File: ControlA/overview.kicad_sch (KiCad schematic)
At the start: 0 parts

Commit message: add libray symbole and add sheet
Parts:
- added C? (x2): 100n, symbol Device:C
- added C? (x2): C_Polarized_US, symbol Device:C_Polarized_US
- added D?: LED, symbol Device:LED
- added D?: SMAJ6.0CA, SMAJ6.0CA:DIOM4325X250N, symbol SMAJ60CA:SMAJ6.0CA
- added J?: XT30PW-M, XT30PW-M:AMASS_XT30PW-M, symbol XT30PW_M:XT30PW-M
- added R? (x2): 2K2, symbol Device:R
- added R? (x2): 39K, symbol Device:R
- added TH?: 10K, symbol Device:Thermistor_NTC
- added U?: XH-2PWBPZ, symbol XH-2PWBPZ:XH-2PWBPZ
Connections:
- new net: D?.2 (A), R?.2
- new net +3V3: C?.1, R?.1, U?.1
- new net +VDC: C?.1, C?.1, D?.1, J?.P, R?.1, R?.1
- new net ADC_TEMP: R?.2, TH?.1, U?.2
- new net AN_JN: C?.1, R?.1, R?.2
- new net GND: C?.2, C?.2, C?.2, C?.2, D?.1 (K), D?.2, J?.N, R?.2, TH?.2
- no-connect marks 0 -> 2
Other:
- note added: "BULK CAPACITANCE"
- note added: "CAN BE USED AS SENSOR ON THE BOARD OR SENSOR ON THE MOTOR"
- note added: "ESD SURGE PROTECTION"
- note added: "LED GREEN -POWER ON INDICATOR"
- note added: "NTC THERMISTOR"
- note added: "VOLTAGE_DIVIDER"
- note added: "WHEN: VDC=60V => AN_JN = 3V204"
- note added: "place as close as possible to THE DRIVER MOSFETS"
- note added: "place as close as possible to connector"

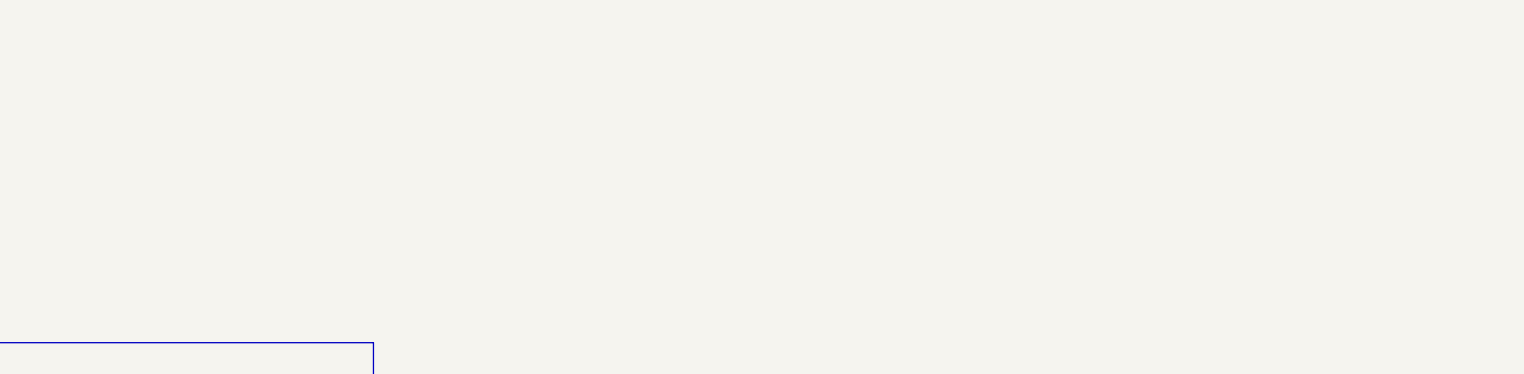
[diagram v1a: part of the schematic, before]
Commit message: shema input protection final
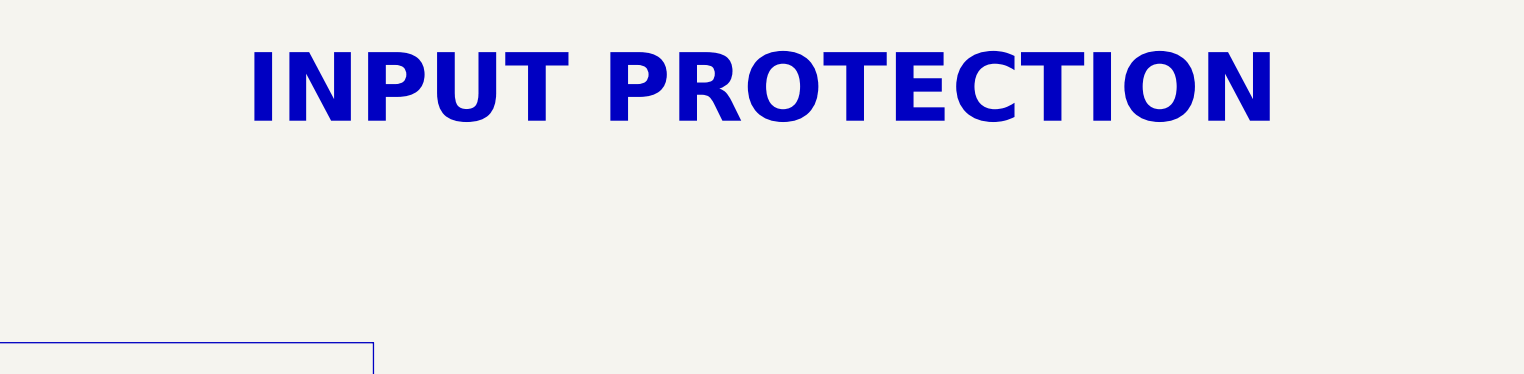
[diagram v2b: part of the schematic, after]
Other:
- note added: "INPUT PROTECTION"
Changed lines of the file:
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@@
+		)
+	)
+	(text "INPUT PROTECTION "
+		(exclude_from_sim no)
+		(at 146.05 35.56 0)
+		(effects
+			(font
+				(face "Arial Black")
+				(size 7.62 7.62)
+				(bold yes)
+				(color 0 0 0 1)
+			)
 		)
 	)

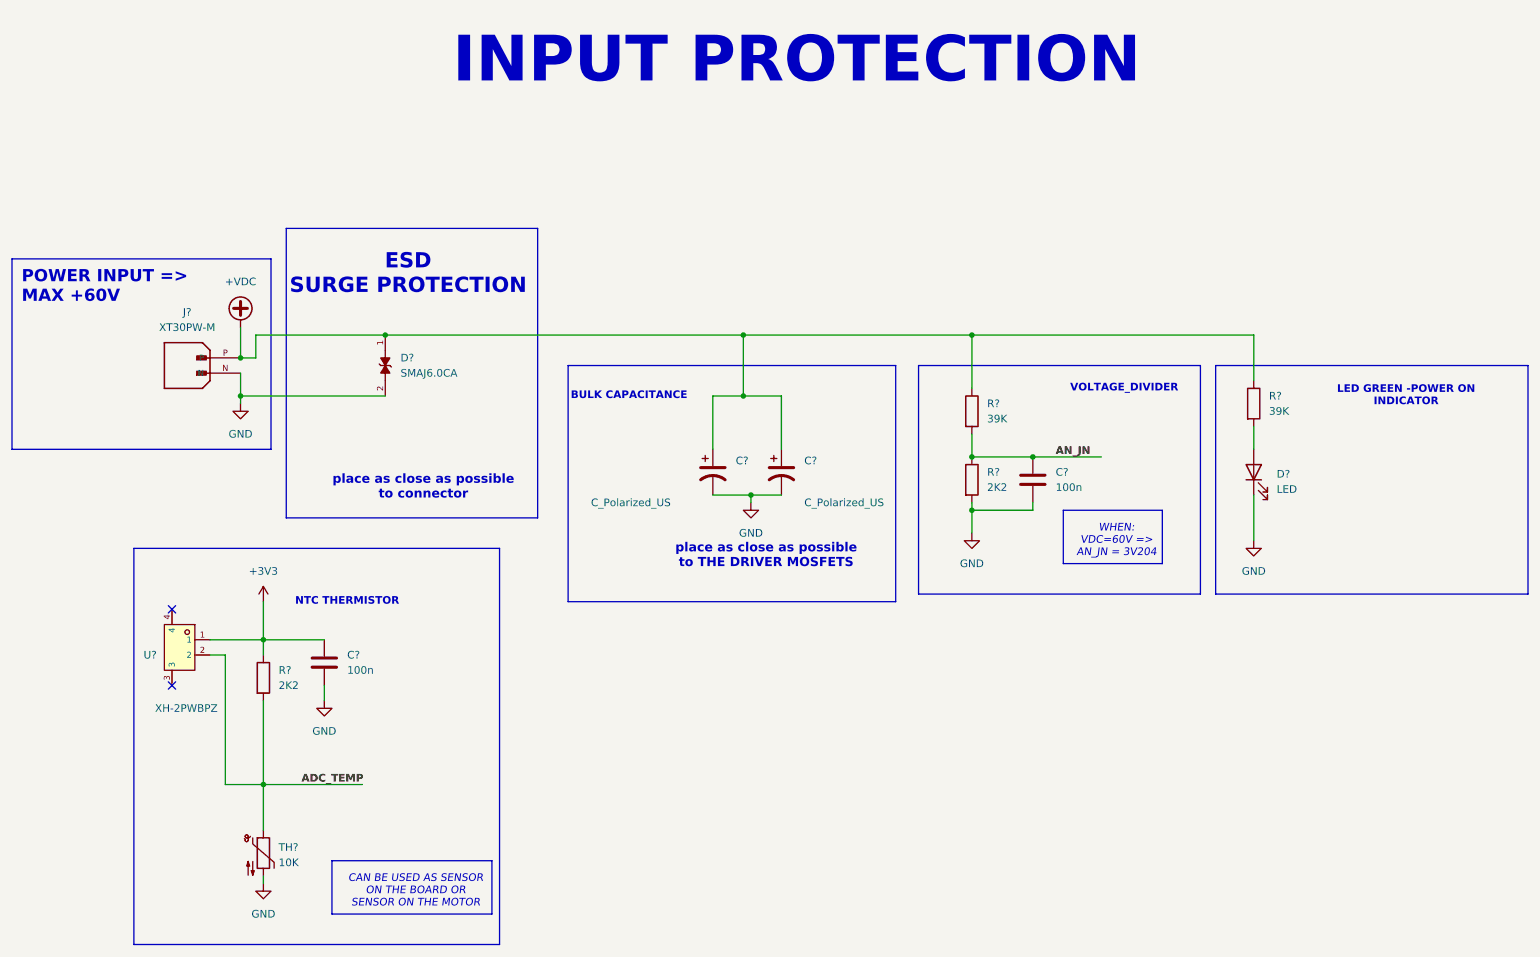
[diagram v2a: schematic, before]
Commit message: final shema symbole
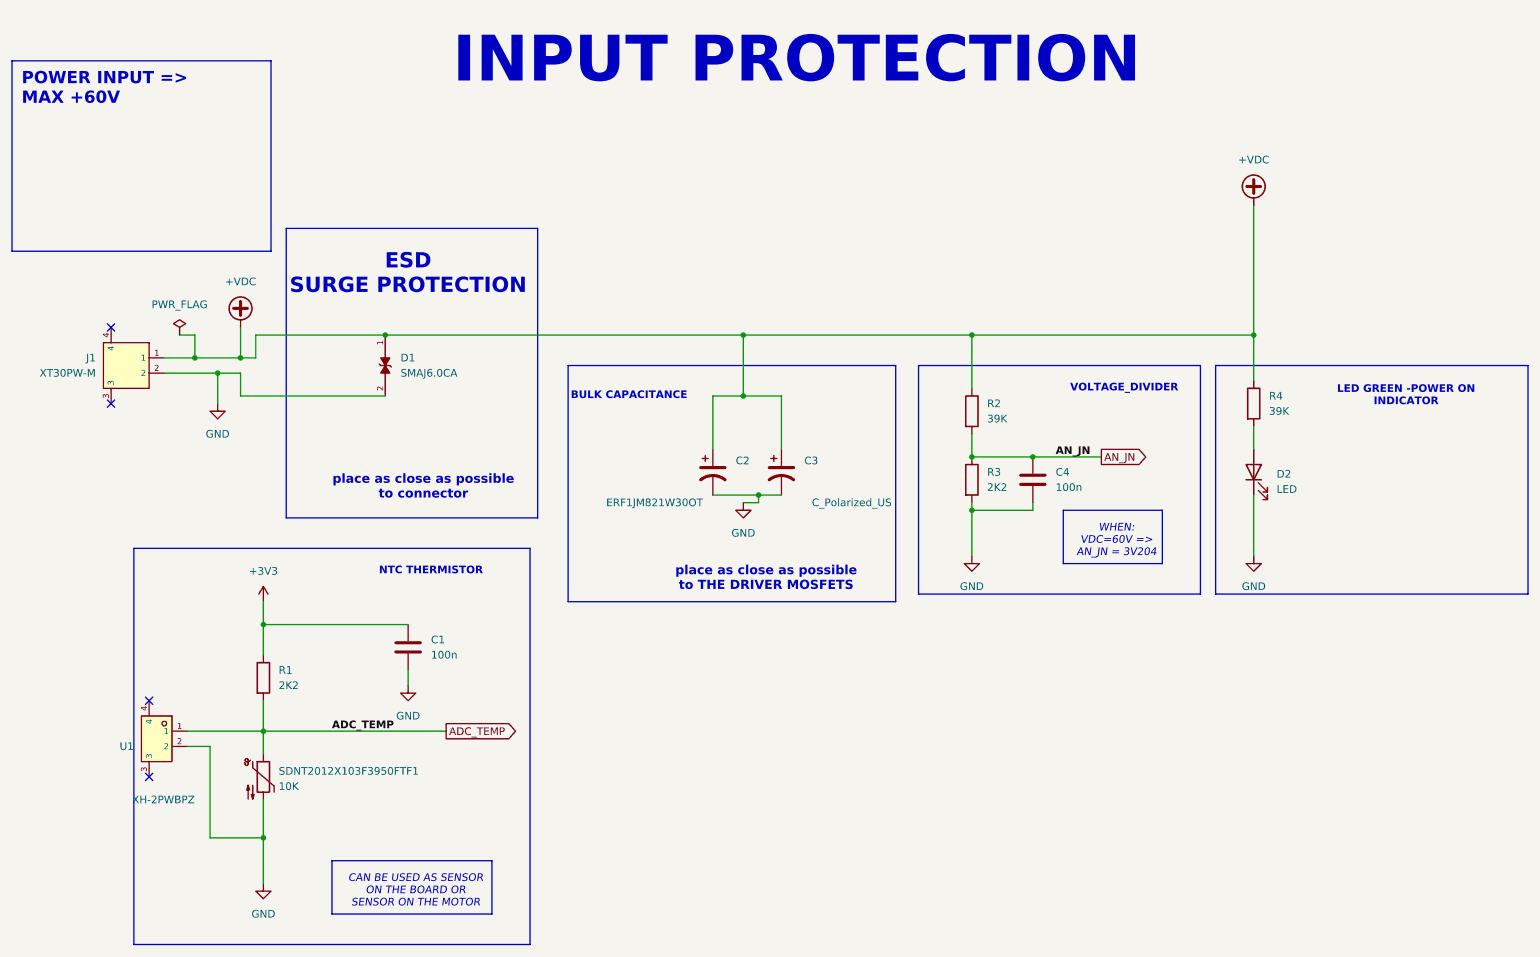
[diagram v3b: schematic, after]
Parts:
- removed C? (x2): C_Polarized_US, symbol Device:C_Polarized_US
- added C2: ERF1JM821W30OT, Capacitor_THT:CP_Radial_D12.5mm_P5.00mm, symbol Device:C_Polarized_US
- added C3: C_Polarized_US, Capacitor_THT:CP_Radial_D12.5mm_P5.00mm, symbol Device:C_Polarized_US
- C1, C4: renamed from C?; footprint (none) -> Capacitor_SMD:C_0805_2012Metric
- D1: renamed from D?; footprint SMAJ6.0CA:DIOM4325X250N -> footprint:DIOM4325X250N
- D2: renamed from D?; footprint (none) -> footprint:LED0805-R-RD
- J1: renamed from J?; footprint XT30PW-M:AMASS_XT30PW-M -> footprint:CONN-TH_XT30PW-M; LCSC (none) -> C431092
- R1, R2, R3, R4: renamed from R?; footprint (none) -> Resistor_SMD:R_0805_2012Metric
- SDNT2012X103F3950FTF1: renamed from TH?; footprint (none) -> Resistor_SMD:R_0805_2012Metric
- U1: renamed from U?; footprint (none) -> footprint:CONN-SMD_XH-2PWBPZ
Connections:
- net +3V3: no longer U1.1
- net +VDC: now also J1.1, C2.1, C3.1; no longer J1.P
- net ADC_TEMP: now also U1.1; no longer U1.2
- net GND: now also J1.2, U1.2, C2.2, C3.2; no longer J1.N
- no-connect marks 2 -> 4
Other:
- moved on the sheet: C1, SDNT2012X103F3950FTF1, U1

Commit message: test0
FIREST
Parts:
- C3: value C_Polarized_US -> ERF1JM821W30OT
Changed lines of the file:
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@@
 			)
 		)
-		(property "Value" "C_Polarized_US"
+		(property "Value" "ERF1JM821W30OT"
 			(at 148.59 109.22 0)
 			(effects

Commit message: CHANGE V11
change v1
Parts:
- C4: footprint Capacitor_SMD:C_0805_2012Metric -> Capacitor_SMD:C_0603_1608Metric
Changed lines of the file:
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@@
-	(wire
-		(pts
-			(xy 137.16 109.22) (xy 139.7 109.22)
-		)
-		(stroke
-			(width 0)
-			(type default)
-		)
-	)
 	(wire
 		(pts
@@
 	(wire
 		(pts
+			(xy 57.15 165.1) (xy 57.15 172.72)
+		)
+		(stroke
+			(width 0)
+			(type default)
+		)
+	)
+	(wire
+		(pts
 			(xy 137.16 81.28) (xy 175.26 81.28)
 		)
@@
 	(wire
 		(pts
-			(xy 139.7 109.22) (xy 139.7 107.95)
+			(xy 139.7 111.76) (xy 139.7 107.95)
 		)
 		(stroke
@@
 		(pts
 			(xy 45.72 85.09) (xy 53.34 85.09)
-		)
-		(stroke
-			(width 0)
-			(type default)
-		)
-	)
-	(wire
-		(pts
-			(xy 57.15 165.1) (xy 57.15 172.72)
 		)
 		(stroke
@@
 	)
 	(symbol
-		(lib_id "power:GND")
-		(at 57.15 172.72 0)
-		(unit 1)
-		(exclude_from_sim no)
-		(in_bom yes)
-		(on_board yes)
-		(dnp no)
-		(fields_autoplaced yes)
-		(property "Reference" "#PWR059"
-			(at 57.15 179.07 0)
-			(effects
-				(font
-					(size 1.27 1.27)
-				)
-				(hide yes)
-			)
-		)
-		(property "Value" "GND"
-			(at 57.15 177.8 0)
-			(effects
-				(font
-					(size 1.27 1.27)
-				)
-			)
-		)
-		(property "Footprint" ""
-			(at 57.15 172.72 0)
-			(effects
-				(font
-					(size 1.27 1.27)
-				)
-				(hide yes)
-			)
-		)
-		(property "Datasheet" ""
-			(at 57.15 172.72 0)
-			(effects
-				(font
-					(size 1.27 1.27)
-				)
-				(hide yes)
-			)
-		)
-		(property "Description" "Power symbol creates a global label with name \"GND\" , ground"
-			(at 57.15 172.72 0)
-			(effects
-				(font
-					(size 1.27 1.27)
-				)
-				(hide yes)
-			)
-		)
-		(pin "1"
-		)
-		(instances
-			(project "ControlA"
-				(path "/28f77b05-53a5-4f29-9b4d-d18dbf030970/8b90f1aa-83f4-48c7-b45b-eecece8cbc1b"
-					(reference "#PWR059")
-					(unit 1)
-				)
-			)
-		)
-	)
-	(symbol
 		(lib_id "Device:C_Polarized_US")
 		(at 143.51 104.14 0)
@@
 	(symbol
 		(lib_id "power:GND")
-		(at 137.16 109.22 0)
+		(at 139.7 111.76 0)
 		(unit 1)
 		(exclude_from_sim no)
@@
 		(fields_autoplaced yes)
 		(property "Reference" "#PWR056"
-			(at 137.16 115.57 0)
+			(at 139.7 118.11 0)
 			(effects
 				(font
@@
 		)
 		(property "Value" "GND"
-			(at 137.16 114.3 0)
+			(at 139.7 116.84 0)
 			(effects
 				(font
@@
 		)
 		(property "Footprint" ""
-			(at 137.16 109.22 0)
+			(at 139.7 111.76 0)
 			(effects
 				(font
@@
 		)
 		(property "Datasheet" ""
-			(at 137.16 109.22 0)
+			(at 139.7 111.76 0)
 			(effects
 				(font
@@
 		)
 		(property "Description" "Power symbol creates a global label with name \"GND\" , ground"
-			(at 137.16 109.22 0)
+			(at 139.7 111.76 0)
 			(effects
 				(font
@@
 	)
 	(symbol
+		(lib_id "power:GND")
+		(at 57.15 172.72 0)
+		(unit 1)
+		(exclude_from_sim no)
+		(in_bom yes)
+		(on_board yes)
+		(dnp no)
+		(fields_autoplaced yes)
+		(property "Reference" "#PWR054"
+			(at 57.15 179.07 0)
+			(effects
+				(font
+					(size 1.27 1.27)
+				)
+				(hide yes)
+			)
+		)
+		(property "Value" "GND"
+			(at 57.15 177.8 0)
+			(effects
+				(font
+					(size 1.27 1.27)
+				)
+			)
+		)
+		(property "Footprint" ""
+			(at 57.15 172.72 0)
+			(effects
+				(font
+					(size 1.27 1.27)
+				)
+				(hide yes)
+			)
+		)
+		(property "Datasheet" ""
+			(at 57.15 172.72 0)
+			(effects
+				(font
+					(size 1.27 1.27)
+				)
+				(hide yes)
+			)
+		)
+		(property "Description" "Power symbol creates a global label with name \"GND\" , ground"
+			(at 57.15 172.72 0)
+			(effects
+				(font
+					(size 1.27 1.27)
+				)
+				(hide yes)
+			)
+		)
+		(pin "1"
+		)
+		(instances
+			(project "ControlA"
+				(path "/28f77b05-53a5-4f29-9b4d-d18dbf030970/8b90f1aa-83f4-48c7-b45b-eecece8cbc1b"
+					(reference "#PWR054")
+					(unit 1)
+				)
+			)
+		)
+	)
+	(symbol
 		(lib_id "Device:C_Polarized_US")
 		(at 132.08 104.14 0)
@@
 			)
 		)
-		(property "Footprint" "Capacitor_SMD:C_0805_2012Metric"
+		(property "Footprint" "Capacitor_SMD:C_0603_1608Metric"
 			(at 186.3852 109.22 0)
 			(effects

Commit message: connector
add conctor power mosft
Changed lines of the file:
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@@
+	)
+	(junction
+		(at 50.8 165.1)
+		(diameter 0)
+		(color 0 0 0 0)
 	)
 	(junction
@@
 	)
 	(junction
-		(at 57.15 165.1)
-		(diameter 0)
-		(color 0 0 0 0)
-	)
-	(junction
 		(at 137.16 91.44)
 		(diameter 0)
@@
 	(wire
 		(pts
-			(xy 57.15 165.1) (xy 57.15 172.72)
+			(xy 50.8 165.1) (xy 50.8 172.72)
 		)
 		(stroke
@@
 	(wire
 		(pts
-			(xy 48.26 165.1) (xy 57.15 165.1)
+			(xy 50.8 165.1) (xy 57.15 165.1)
+		)
+		(stroke
+			(width 0)
+			(type default)
+		)
+	)
+	(wire
+		(pts
+			(xy 48.26 165.1) (xy 50.8 165.1)
 		)
 		(stroke
@@
 	(symbol
 		(lib_id "power:GND")
-		(at 57.15 172.72 0)
+		(at 50.8 172.72 0)
 		(unit 1)
 		(exclude_from_sim no)
@@
 		(fields_autoplaced yes)
 		(property "Reference" "#PWR054"
-			(at 57.15 179.07 0)
+			(at 50.8 179.07 0)
 			(effects
 				(font
@@
 		)
 		(property "Value" "GND"
-			(at 57.15 177.8 0)
+			(at 50.8 177.8 0)
 			(effects
 				(font
@@
 		)
 		(property "Footprint" ""
-			(at 57.15 172.72 0)
+			(at 50.8 172.72 0)
 			(effects
 				(font
@@
 		)
 		(property "Datasheet" ""
-			(at 57.15 172.72 0)
+			(at 50.8 172.72 0)
 			(effects
 				(font
@@
 		)
 		(property "Description" "Power symbol creates a global label with name \"GND\" , ground"
-			(at 57.15 172.72 0)
-			(effects
-				(font
+			(at 50.8 172.72 0)
+			(effects
+				(font
